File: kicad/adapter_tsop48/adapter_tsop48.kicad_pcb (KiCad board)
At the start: 2 copper layers, 48 x 33 mm, 3 parts, among them J1 Conn_02x12_Odd_Even_1, J2 Conn_02x12_Odd_Even_2, P1 TSOP-48_adapter

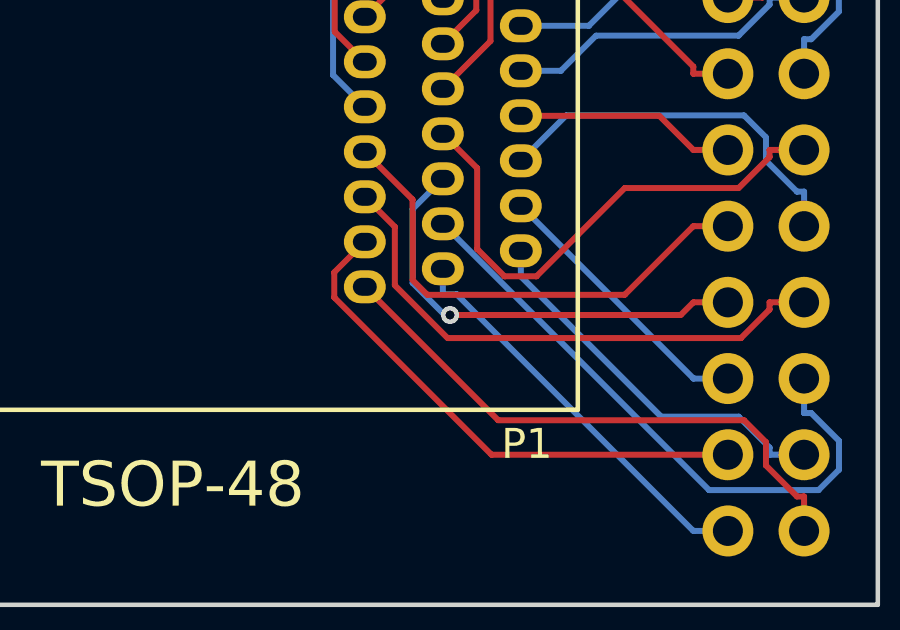
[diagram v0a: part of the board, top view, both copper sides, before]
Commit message: Migrate mainboard and adapter_tsop48 to kicad 10 and various changes
Replace the regulator with an AMS1117-3.3 and change the USB port to a generic USB-C port.
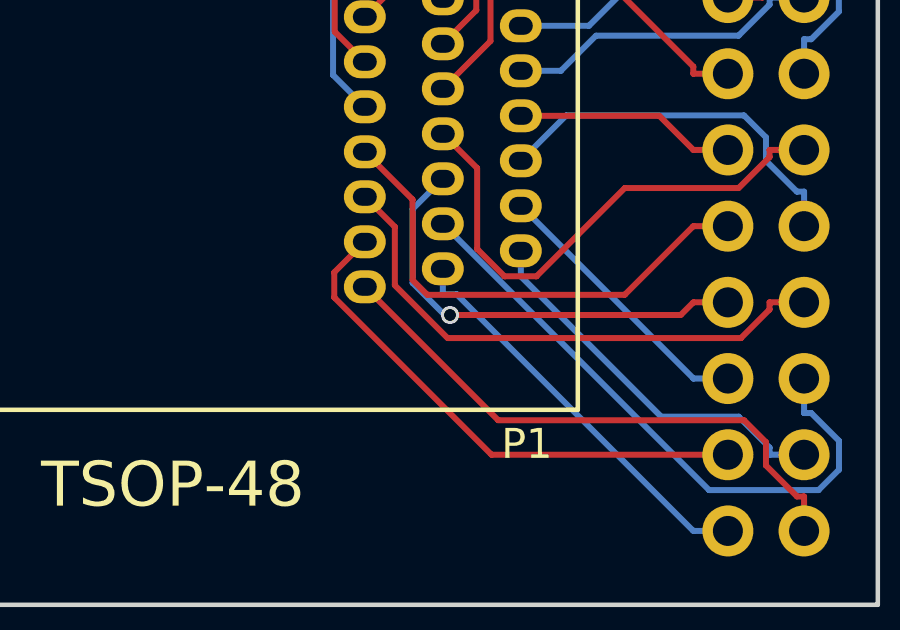
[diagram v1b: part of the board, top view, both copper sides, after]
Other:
- net class Default removed

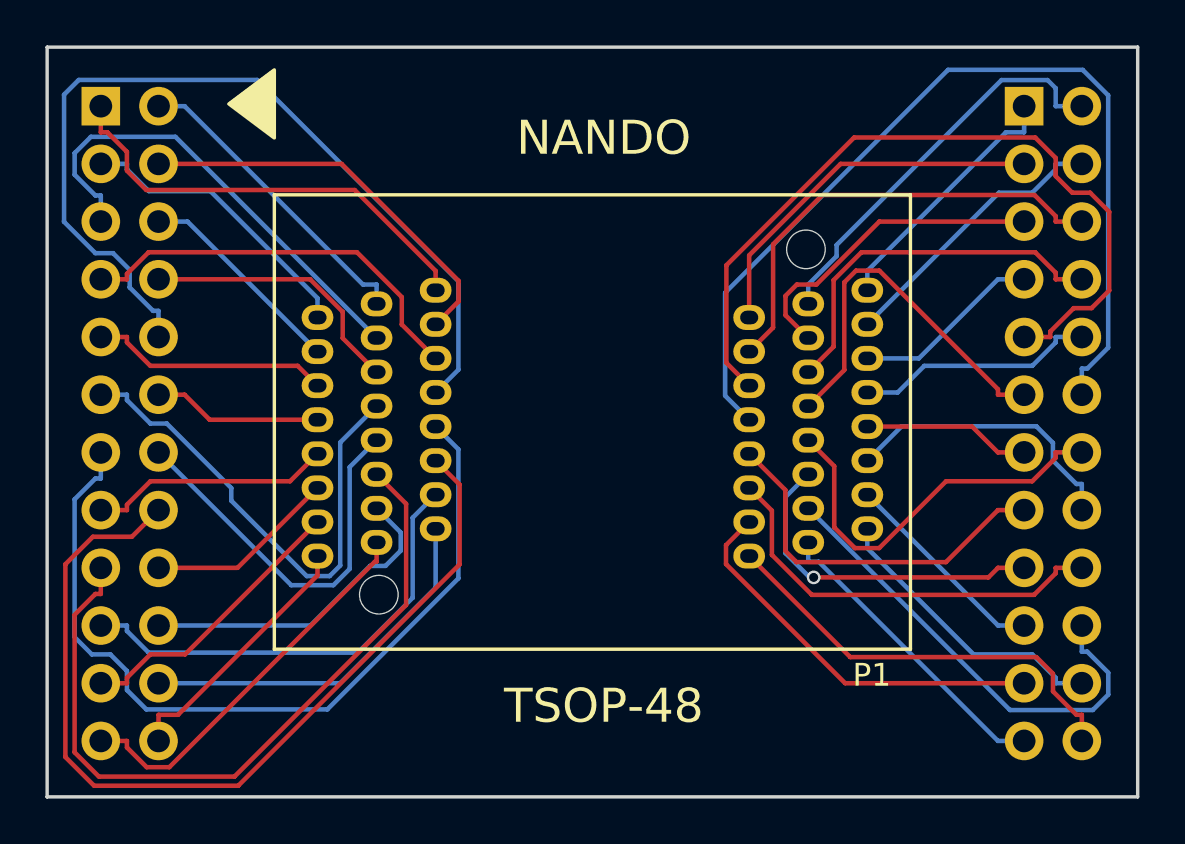
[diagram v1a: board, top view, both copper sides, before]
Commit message: Add LCSC metadata to adapter_tsop48
This is used only for preconfigured gerber export and not for PCBA.
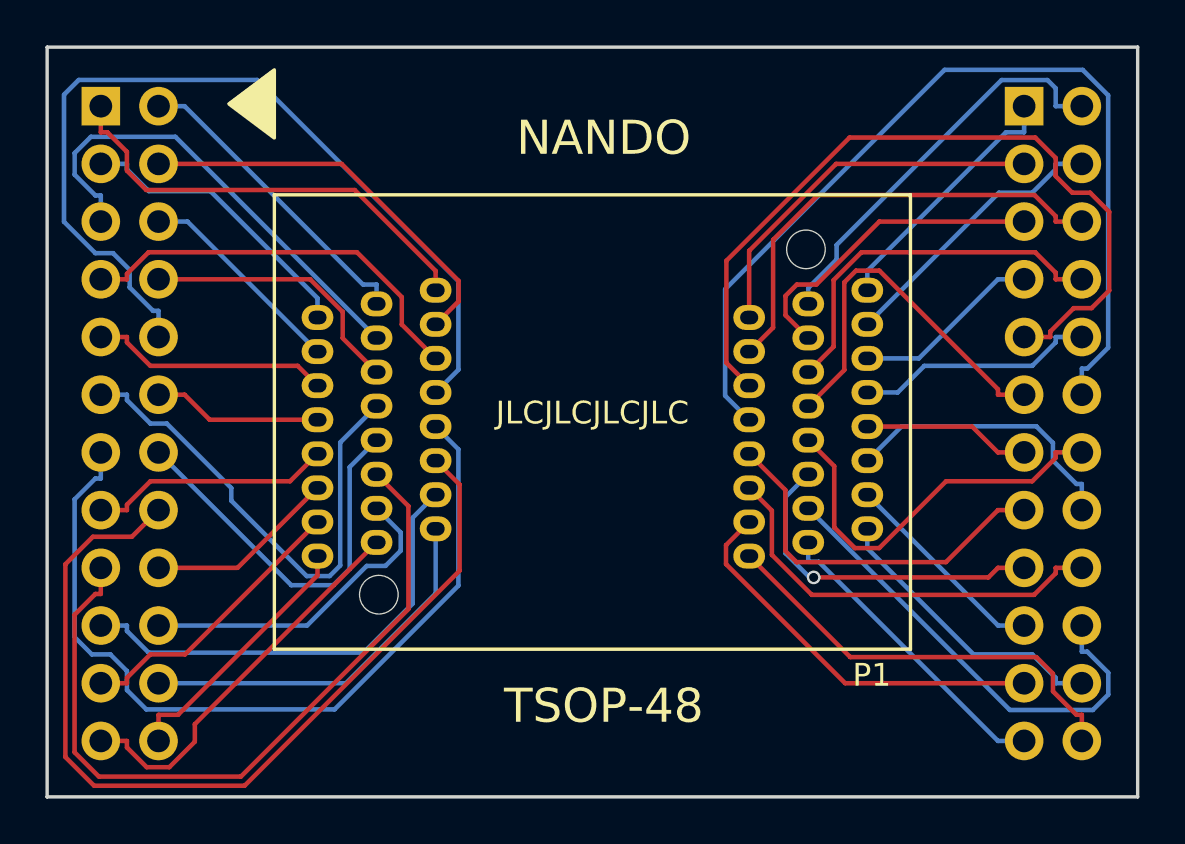
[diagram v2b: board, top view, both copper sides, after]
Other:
- rule pad_to_mask_clearance: 0.2 -> 0
- board text added: "JLCJLCJLCJLC"
